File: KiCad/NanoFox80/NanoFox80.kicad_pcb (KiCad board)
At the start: 2 copper layers, 90 x 37 mm, 72 parts, among them J101 Conn_01x02, J102 Conn_01x02, J103 Conn_01x01, J104 Conn_01x02, J105 Conn_01x02, J106 Conn_01x02, J107 Conn_01x02, J108 Conn_01x01, J109 Conn_01x02, J110 I2C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

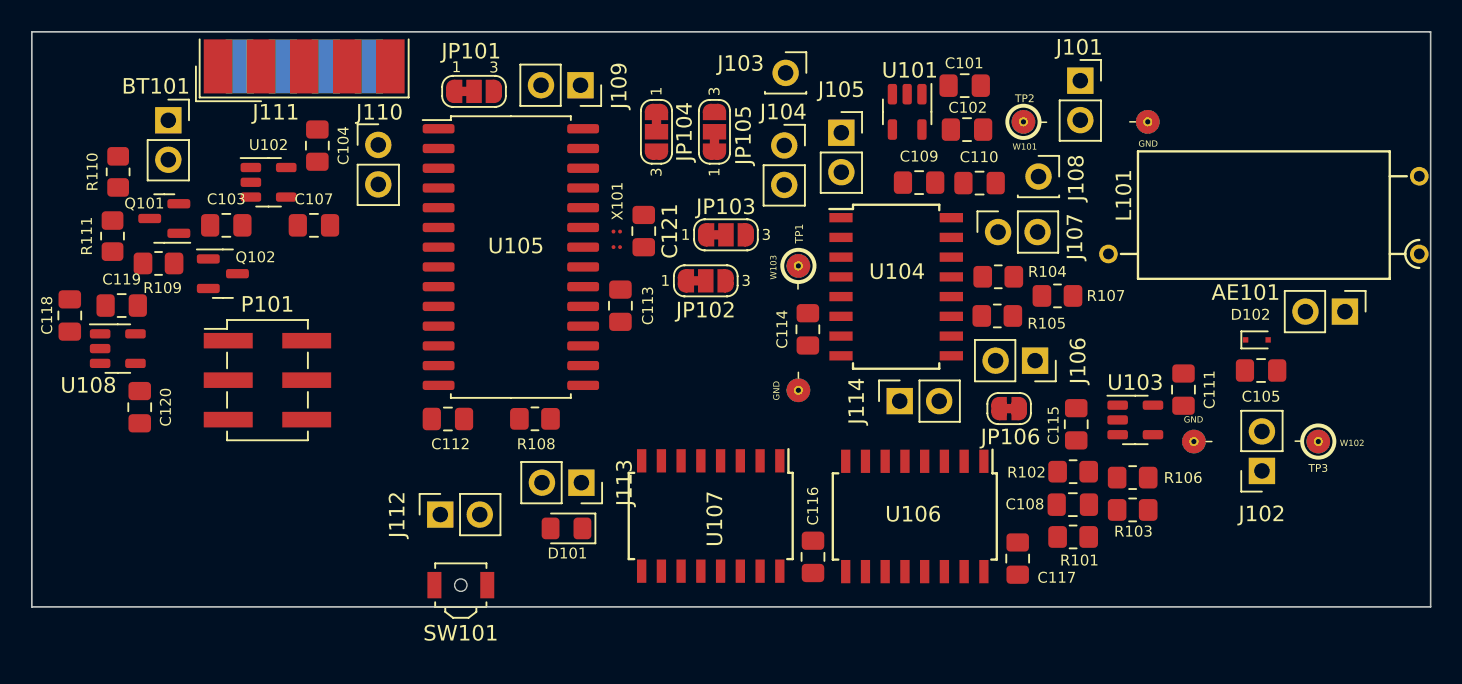
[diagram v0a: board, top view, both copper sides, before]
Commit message: Parts Update
Changed LED to be a right-angle device
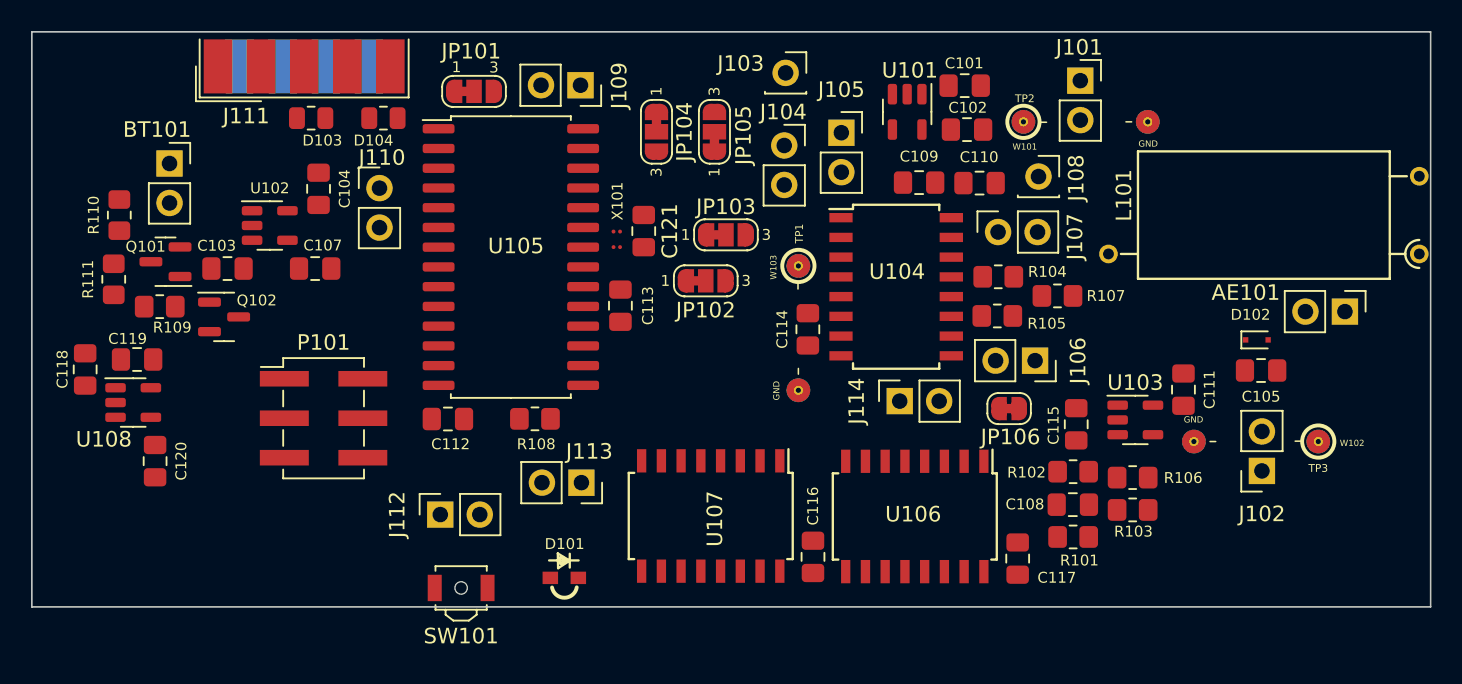
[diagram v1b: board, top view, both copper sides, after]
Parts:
- added D103: CG0603MLC-05LECT-ND, Resistor_SMD:R_0805_2012Metric, F.Cu at (98.0, 61.5)
- added D104: CG0603MLC-05LECT-ND, Resistor_SMD:R_0805_2012Metric, F.Cu at (102.6, 61.5)
- C105: value 100pF -> 220pF
- D101: footprint LED_SMD:LED_0805_2012Metric_Pad1.15x1.40mm_HandSolder -> LED_SMD:LED_APDA1806SECK
- moved P101 4.36 mm to (98.8, 80.9)
- moved C118 3.61 mm to (83.4, 77.7)
- moved C120 3.61 mm to (87.9, 83.6)
- moved C119 3.61 mm to (86.8, 77.1)
- moved U108 3.61 mm to (86.5, 79.8)
- moved D101 3.18 mm to (114.3, 91.1)
- moved BT101 2.78 mm to (88.9, 64.5)
- moved C103 2.78 mm to (92.6, 71.2)
- moved C107 2.78 mm to (98.2, 71.2)
- moved Q101 2.78 mm to (88.6, 70.8)
- moved Q102 2.78 mm to (92.4, 74.3)
- moved R109 2.78 mm to (88.2, 73.7)
- moved R110 2.78 mm to (85.6, 67.8)
- moved R111 2.78 mm to (85.3, 71.9)
- moved C104 2.78 mm to (98.4, 66.1)
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
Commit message: Updated Schematic & PCB
o Corrected varactor circuit
o Added level translation to USART
o Added mounting holes to PCB
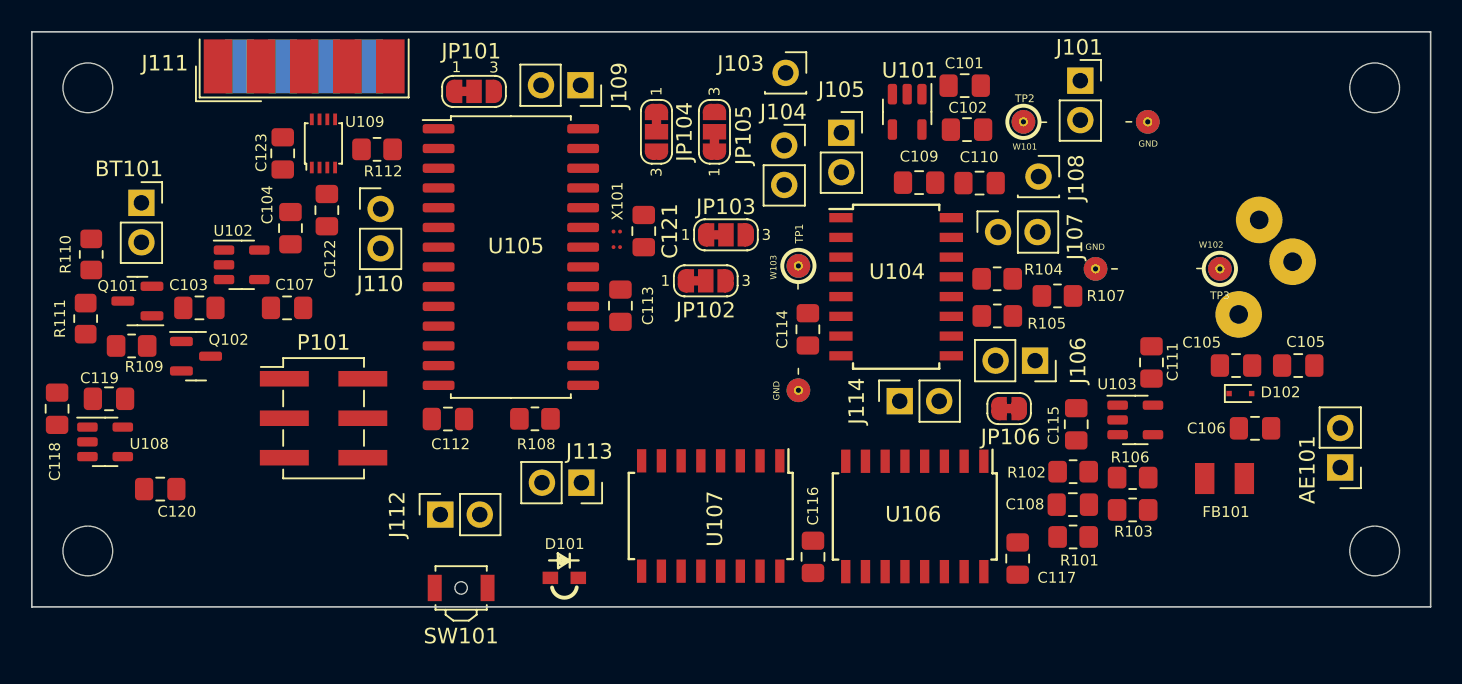
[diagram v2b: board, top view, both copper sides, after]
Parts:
- removed D103, D104: CG0603MLC-05LECT-ND, Resistor_SMD:R_0805_2012Metric
- removed J102: Conn_01x02, Connector_PinSocket_2.54mm:PinSocket_1x02_P2.54mm_Vertical
- added C105: 220pF, Capacitor_SMD:C_0805_2012Metric_Pad1.18x1.45mm_HandSolder, F.Cu at (161.5, 77.5)
- added C106: 470nF, Capacitor_SMD:C_0805_2012Metric_Pad1.18x1.45mm_HandSolder, F.Cu at (158.7, 81.5)
- added C122: 470nF, Capacitor_SMD:C_0805_2012Metric_Pad1.18x1.45mm_HandSolder, F.Cu at (99.0, 67.5)
- added C123: 470nF, Capacitor_SMD:C_0805_2012Metric_Pad1.18x1.45mm_HandSolder, F.Cu at (96.1, 63.8)
- added FB101: FerriteBead_Small, Inductor_SMD:Ferrite_Bead_NFZ32BW881_Reflow, F.Cu at (156.7, 84.7)
- added R112: 100k, Resistor_SMD:R_0805_2012Metric_Pad1.20x1.40mm_HandSolder, F.Cu at (102.2, 63.6)
- added REF**: MountingHole_3.2mm_M3, MountingHole:MountingHole_3.2mm_M3, F.Cu at (166.4, 59.6)
- added REF**: MountingHole_3.2mm_M3, MountingHole:MountingHole_3.2mm_M3, F.Cu at (166.4, 89.4)
- added REF**: MountingHole_3.2mm_M3, MountingHole:MountingHole_3.2mm_M3, F.Cu at (83.6, 89.4)
- added REF**: MountingHole_3.2mm_M3, MountingHole:MountingHole_3.2mm_M3, F.Cu at (83.6, 59.6)
- added U109: TXB0102DCU, Package_SO:VSSOP-8_2.4x2.1mm_P0.5mm, F.Cu at (98.8, 63.2)
- L101: footprint Transformer_THT:Autotransformer_ZS1052-AC -> Transformer_THT:Autotransformer_Toroid_1Tap_Horizontal_D14.0mm_Amidon-T50; moved to B.Cu
- moved W102 12.8 mm to (156.4, 71.2)
- moved L101 10.7 mm to (162.0, 78.1), turned to 90 degrees
- moved AE101 10.0 mm to (164.2, 84.0), turned to 180 degrees
- moved D102 3.61 mm to (157.8, 79.3)
- moved BT101 3.11 mm to (87.0, 67.0)
- moved C103 3.11 mm to (90.8, 73.8)
- moved C104 3.11 mm to (96.6, 68.6)
- moved C107 3.11 mm to (96.4, 73.8)
- moved C118 3.11 mm to (81.6, 80.2)
- moved Q102 3.11 mm to (90.6, 76.9)
- moved R111 3.11 mm to (83.5, 74.5)
- moved U102 3.11 mm to (93.5, 71.0)
- moved C119 3.11 mm to (85.0, 79.6)
- moved U108 3.11 mm to (84.7, 82.4)
- moved R109 3.11 mm to (86.4, 76.2)
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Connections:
- J111 pad 7: unconnected-(J111-Pad7) -> Net-(J111-Pad7)
- J111 pad 8: Net-(D103-Pad1) -> Net-(J111-Pad8)
- J111 pad 9: Net-(D104-Pad2) -> Net-(J111-Pad9)
- U105 pad 12: Net-(D102-Pad1) -> Net-(U105-Pad12)
- U105 pad 2: Net-(D104-Pad2) -> Net-(U105-Pad2)
- U105 pad 3: Net-(D103-Pad1) -> Net-(U105-Pad3)
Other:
- board text added: "FT-50-67 FT-82-67"

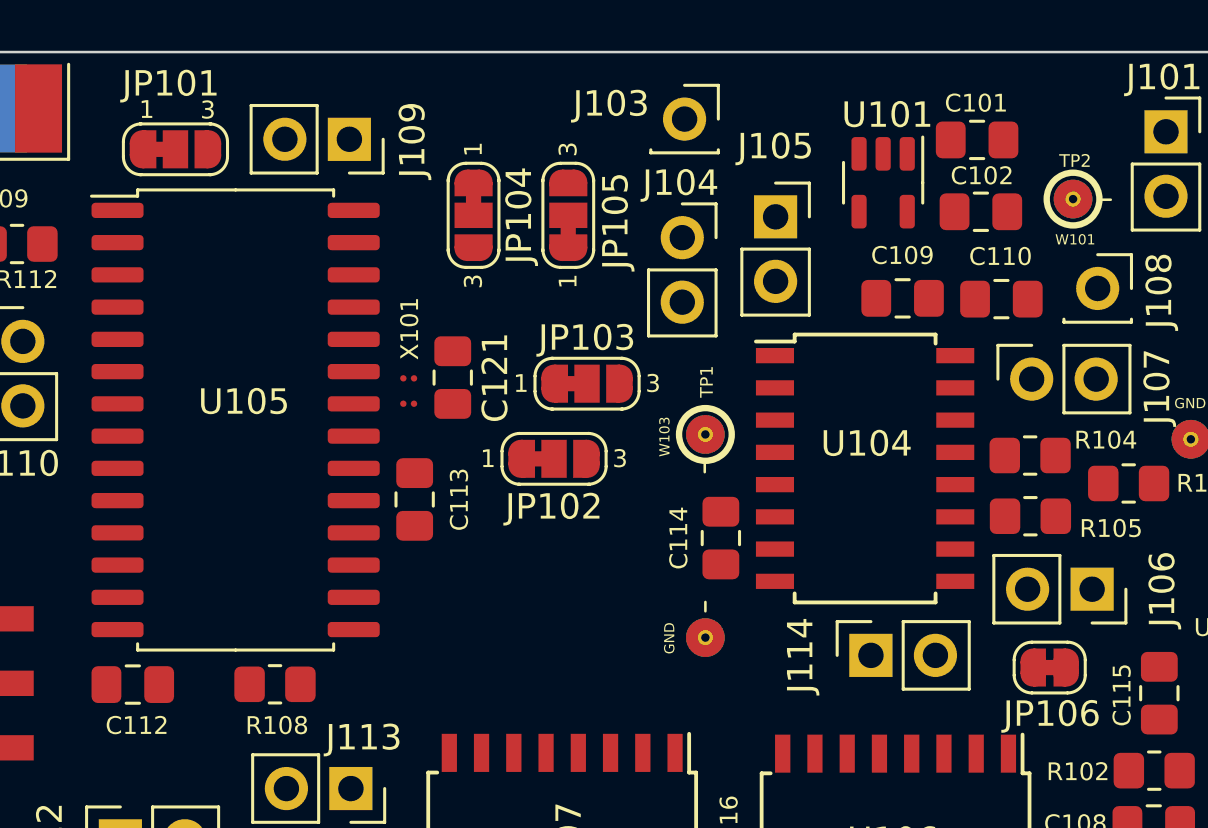
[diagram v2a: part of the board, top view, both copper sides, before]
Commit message: Schematic Update
Updated L101 information
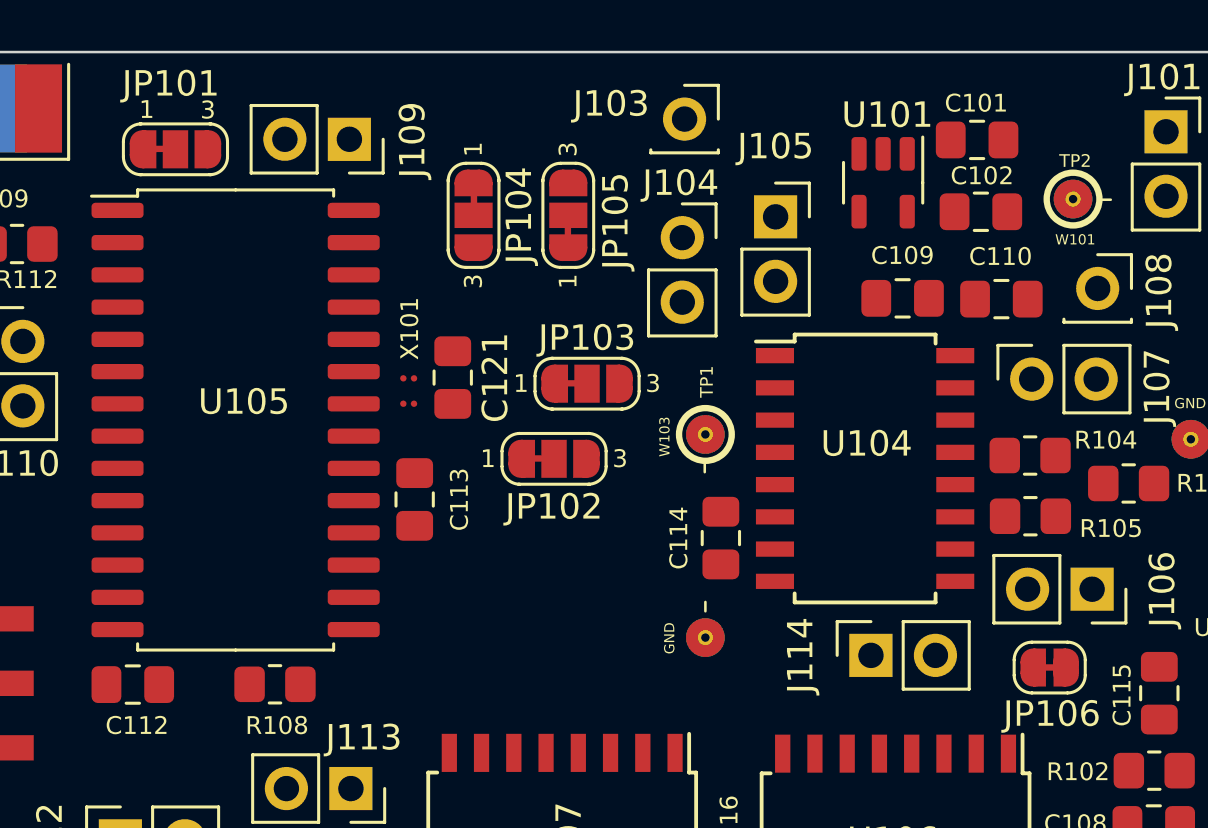
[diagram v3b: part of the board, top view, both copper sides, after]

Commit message: PCB Routed
o First cut at PCB board
o Gerbers updated
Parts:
- J111: moved to B.Cu
- moved J111 22.5 mm to (82.0, 74.5), turned to 90 degrees
- moved R112 20.7 mm to (87.0, 77.7)
- moved P101 16.1 mm to (94.9, 65.2), turned to 180 degrees
- moved U109 16.0 mm to (86.4, 73.3), turned to 180 degrees
- moved U108 15.2 mm to (97.9, 90.0)
- moved C118 15.2 mm to (94.8, 87.8)
- moved C119 15.2 mm to (98.1, 87.2)
- moved C123 14.9 mm to (87.0, 75.6), turned to 180 degrees
- moved C120 14.8 mm to (101.9, 91.2)
- moved W102 11.9 mm to (167.0, 76.7), turned to -90 degrees
- moved BT101 11.0 mm to (95.5, 74.0)
- moved R110 10.6 mm to (91.5, 77.7), turned to 0 degrees
- moved C122 10.00 mm to (90.7, 73.0), turned to 0 degrees
- moved R109 9.72 mm to (93.2, 83.2)
- moved Q102 9.68 mm to (97.2, 83.9)
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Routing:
- net GND: track 0.00 -> 321.5 mm, vias 0 -> 210
- net +5V: track 0.00 -> 115.2 mm, vias 0 -> 7
- net +3V3: track 0.00 -> 67.4 mm, vias 0 -> 6
- net Net-(U105-Pad12): track 0.00 -> 56.2 mm, vias 0 -> 4
- net Enable_5V: track 0.00 -> 38.8 mm
- net +BATT: track 0.00 -> 36.8 mm, vias 0 -> 2
- net Net-(JP103-Pad3): track 0.00 -> 33.9 mm, vias 0 -> 3
- net Enable_Vdiv: track 0.00 -> 32.0 mm, vias 0 -> 2
- net Net-(JP102-Pad1): track 0.00 -> 31.2 mm
- net Net-(U104-Pad5): track 0.00 -> 30.6 mm, vias 0 -> 2
- net Net-(U105-Pad3): track 0.00 -> 28.9 mm
- net Net-(U101-Pad4): track 0.00 -> 28.5 mm
- net Net-(R103-Pad2): track 0.00 -> 28.2 mm
- net Net-(U105-Pad2): track 0.00 -> 27.9 mm, vias 0 -> 2
- net Net-(U101-Pad3): track 0.00 -> 25.1 mm, vias 0 -> 2
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- added copper zone on B.Cu, net GND
- added copper zone on F.Cu, net GND
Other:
- board text added: "Fout"
- board text added: "NanoFox80 Rev: 30-Apr-2022"
- board text added: "RF"
- board text added: "U101-Out"

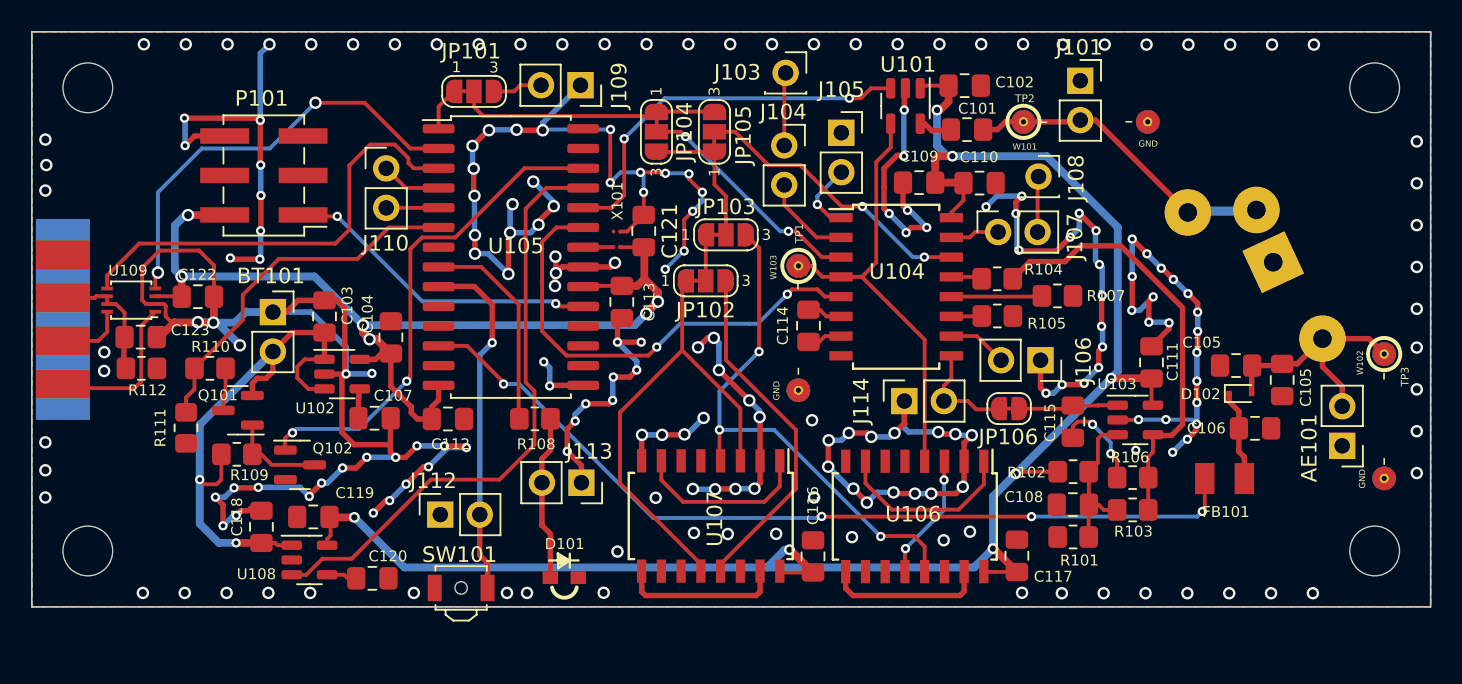
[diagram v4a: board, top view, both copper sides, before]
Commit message: PCB Updates
o Added better silkscreen to X101
o More stitch vias
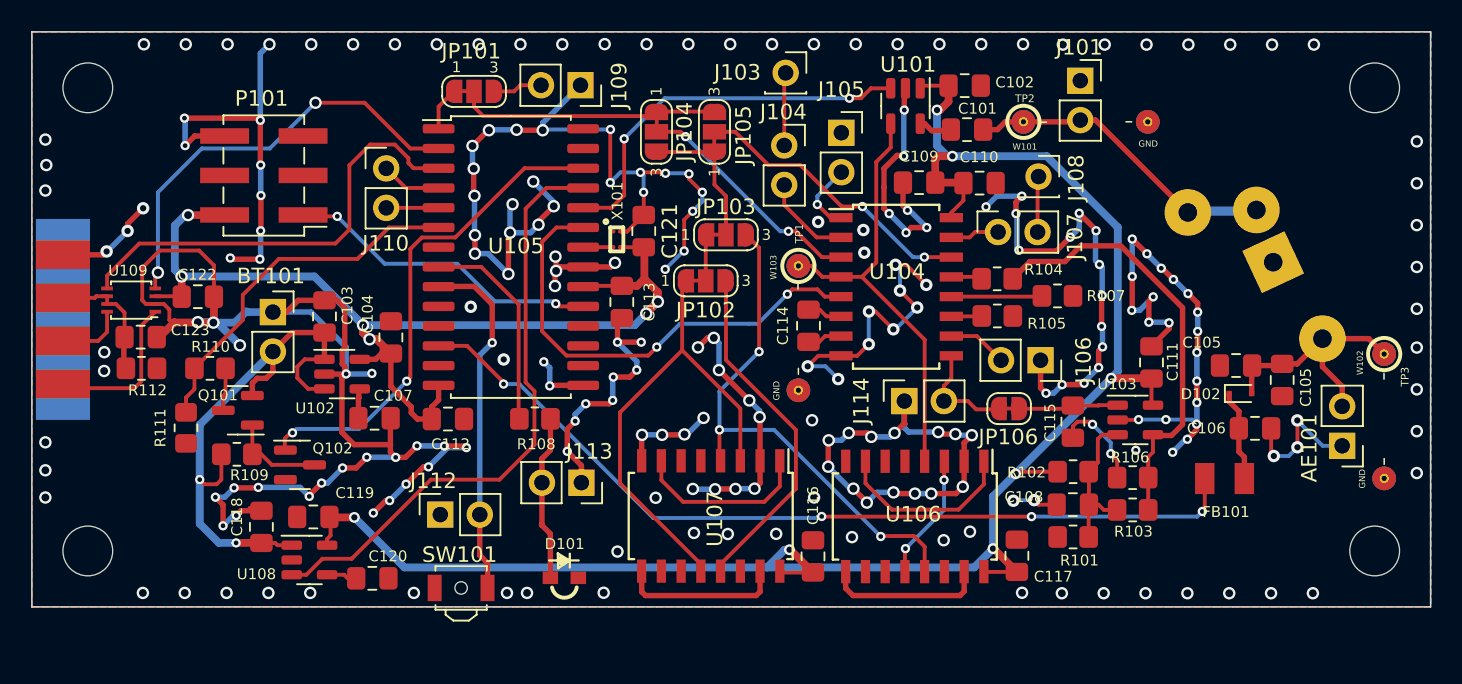
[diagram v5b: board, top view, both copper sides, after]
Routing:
- net GND: track 321.5 -> 359.0 mm, vias 210 -> 232
